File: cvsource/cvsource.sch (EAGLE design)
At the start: 114 parts, among them IC1 OPA4130P, IC2 OPA2134P, IC3 78L05Z, P1 US-EVUF3J, P2 US-EVUF3J, P3 US-EVUF3J, P4 US-EVUF3J, X1 2516-

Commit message: ordered cvsource
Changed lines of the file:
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@@
 <segment>
 <pinref part="CVOUT4" gate="G$1" pin="P$3"/>
-<label x="-160.02" y="-68.58" size="1.778" layer="95"/>
-<wire x1="-157.48" y1="-66.04" x2="-160.02" y2="-66.04" width="0.1524" layer="91"/>
-<wire x1="-160.02" y1="-66.04" x2="-160.02" y2="-71.12" width="0.1524" layer="91"/>
-<wire x1="-160.02" y1="-71.12" x2="-142.24" y2="-71.12" width="0.1524" layer="91"/>
+<label x="-162.56" y="-68.58" size="1.778" layer="95"/>
+<wire x1="-157.48" y1="-66.04" x2="-162.56" y2="-66.04" width="0.1524" layer="91"/>
+<wire x1="-162.56" y1="-66.04" x2="-162.56" y2="-71.12" width="0.1524" layer="91"/>
+<wire x1="-162.56" y1="-71.12" x2="-142.24" y2="-71.12" width="0.1524" layer="91"/>
 <wire x1="-142.24" y1="-71.12" x2="-142.24" y2="-76.2" width="0.1524" layer="91"/>
 <pinref part="D1" gate="1" pin="AG"/>
@@
 <wire x1="-160.02" y1="-76.2" x2="-162.56" y2="-76.2" width="0.1524" layer="91"/>
 <wire x1="-162.56" y1="-76.2" x2="-162.56" y2="-71.12" width="0.1524" layer="91"/>
-<wire x1="-162.56" y1="-71.12" x2="-160.02" y2="-71.12" width="0.1524" layer="91"/>
-<junction x="-160.02" y="-71.12"/>
+<junction x="-162.56" y="-71.12"/>
 </segment>
 <segment>

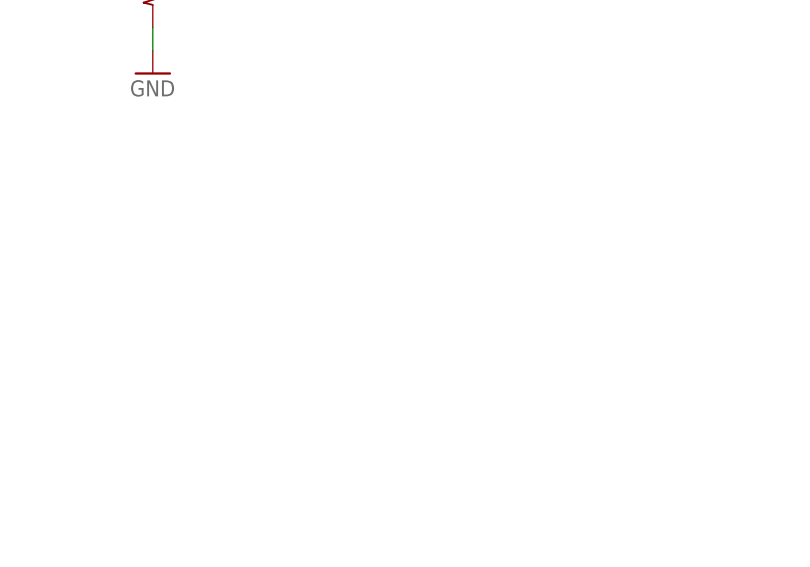
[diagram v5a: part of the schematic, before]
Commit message: got the cv source back from board fab.  added panel.
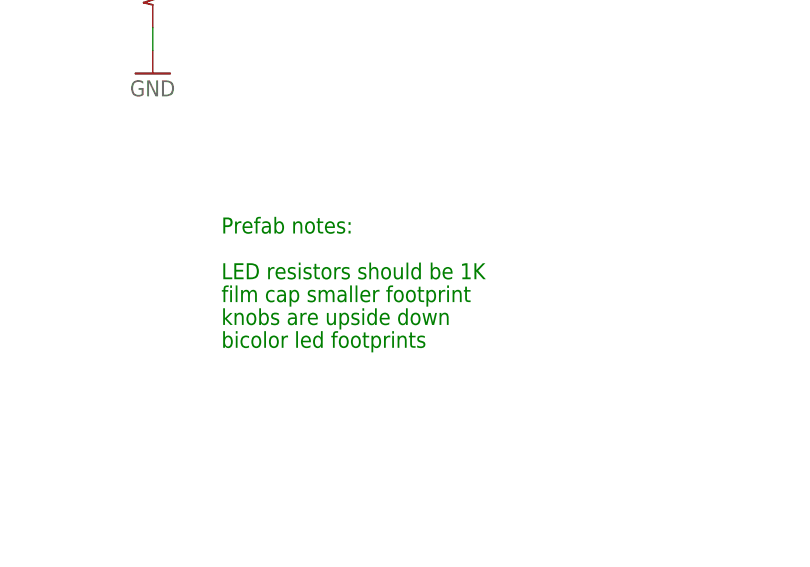
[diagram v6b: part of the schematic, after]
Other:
- note added: "LED resistors should be 1K"
- note added: "Prefab notes:"
- note added: "bicolor led footprints"
- note added: "film cap smaller footprint"
- note added: "knobs are upside down"
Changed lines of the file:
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@@
 <sheet>
 <plain>
+<text x="63.5" y="-50.8" size="1.778" layer="91">Prefab notes:</text>
+<text x="63.5" y="-55.88" size="1.778" layer="91">LED resistors should be 1K</text>
+<text x="63.5" y="-58.42" size="1.778" layer="91">film cap smaller footprint</text>
+<text x="63.5" y="-60.96" size="1.778" layer="91">knobs are upside down</text>
+<text x="63.5" y="-63.5" size="1.778" layer="91">bicolor led footprints</text>
 </plain>
 <instances>
